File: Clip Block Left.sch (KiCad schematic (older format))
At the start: 27 parts, among them J1 Conn_02x05_Odd_Even, SW1 B3F-5050, SW10 B3F-5050, SW11 B3F-5050, SW12 B3F-5050, SW13 B3F-5050, SW14 B3F-5050, SW15 B3F-5050, SW16 B3F-5050, SW2 B3F-5050, SW3 B3F-5050, SW4 B3F-5050, SW5 B3F-5050, SW6 B3F-5050, SW7 B3F-5050, SW8 B3F-5050, SW9 B3F-5050, U1 CD74HC4067M

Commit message: All subsidiary boards complete
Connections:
- wire segments 182 -> 183
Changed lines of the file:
@@
 	1900 2450 2200 2450
-Wire Wire Line
-	1750 2250 2200 2250
 Wire Wire Line
 	2000 1150 2700 1150
@@
 	1    0    0    -1
 $EndComp
-Wire Wire Line
-	1600 2150 2200 2150
-Wire Wire Line
-	1750 2250 1750 1750
-Wire Wire Line
-	1750 1750 900  1750
-Wire Wire Line
-	900  1750 900  2150
-Wire Wire Line
-	900  2150 1100 2150
 Wire Wire Line
 	1700 2350 1700 2250
@@
 NoConn ~ 1900 4300
 NoConn ~ 1900 4800
+Wire Wire Line
+	2200 2150 2200 1900
+Wire Wire Line
+	2200 1900 900  1900
+Wire Wire Line
+	900  1900 900  2150
+Wire Wire Line
+	900  2150 1100 2150
+Wire Wire Line
+	1600 2150 1850 2150
+Wire Wire Line
+	1850 2150 1850 2250
+Wire Wire Line
+	1850 2250 2200 2250
 $EndSCHEMATC

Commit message: Housekeeping
Cleaned up the schematic for the subsidiary boards

Switched 5v and Com connections to make routing easier.
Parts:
- J1: symbol Connector_Generic:Conn_02x05_Odd_Even -> Connector:Conn_01x10_Male
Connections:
- wire segments 183 -> 172
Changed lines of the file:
@@
 	1    0    0    -1
 $EndComp
-Wire Wire Line
-	2100 2550 2100 1750
-Wire Wire Line
-	2100 1750 2200 1750
 Connection ~ 2700 1150
 NoConn ~ 4900 2450
@@
 	2200 3450 2700 3450
 Wire Wire Line
-	1750 2550 2100 2550
-Wire Wire Line
-	1900 2450 2200 2450
-Wire Wire Line
-	2000 1150 2700 1150
-Wire Wire Line
-	2000 1150 2000 2650
-Wire Wire Line
 	2700 1150 2700 1250
 Wire Wire Line
@@
 	2450 5300 2450 6100
 $Comp
-L Connector_Generic:Conn_02x05_Odd_Even J1
+L Connector:Conn_01x10_Male J1
 U 1 1 5D5B6BD9
-P 1300 2350
-F 0 "J1" H 1350 2767 50  0000 C CNN
-F 1 "Conn_02x05_Odd_Even" H 1350 2676 50  0000 C CNN
-F 2 "Connector_PinHeader_2.54mm:PinHeader_2x05_P2.54mm_Vertical" H 1300 2350 50  0001 C CNN
-F 3 "~" H 1300 2350 50  0001 C CNN
-	1    1300 2350
-	1    0    0    -1
-$EndComp
-Wire Wire Line
-	1700 2350 1700 2250
-Wire Wire Line
-	1700 2250 1600 2250
-Wire Wire Line
-	1700 2350 2200 2350
-Wire Wire Line
-	1900 2450 1900 1600
-Wire Wire Line
-	1900 1600 650  1600
-Wire Wire Line
-	650  1600 650  2250
-Wire Wire Line
-	650  2250 1100 2250
-Wire Wire Line
-	1750 2550 1750 2400
-Wire Wire Line
-	1750 2400 1650 2400
-Wire Wire Line
-	1650 2400 1650 2350
-Wire Wire Line
-	1650 2350 1600 2350
-Wire Wire Line
-	950  2650 950  2350
-Wire Wire Line
-	950  2350 1100 2350
-Wire Wire Line
-	950  2650 2000 2650
+P 750 2550
+F 0 "J1" H 750 3100 50  0000 C CNN
+F 1 "Conn_02x05_Odd_Even" H 800 2876 50  0001 C CNN
+F 2 "Connector_PinHeader_2.54mm:PinHeader_2x05_P2.54mm_Vertical" H 750 2550 50  0001 C CNN
+F 3 "~" H 750 2550 50  0001 C CNN
+	1    750  2550
+	1    0    0    -1
+$EndComp
 $Comp
 L Connector_Generic:Conn_02x03_Odd_Even JX01
@@
 NoConn ~ 750  7050
 Wire Wire Line
-	1900 3900 1700 3900
-Wire Wire Line
-	1700 3900 1700 2450
-Wire Wire Line
-	1600 2450 1700 2450
-Wire Wire Line
-	1900 4400 1600 4400
-Wire Wire Line
-	1600 4400 1600 2550
-Wire Wire Line
-	1900 4900 1100 4900
-Wire Wire Line
-	1100 4900 1100 2550
-Wire Wire Line
-	1900 5300 850  5300
-Wire Wire Line
-	850  5300 850  2450
-Wire Wire Line
-	850  2450 1100 2450
+	1900 4400 1800 4400
+Wire Wire Line
+	1900 4900 1700 4900
+Wire Wire Line
+	1900 5300 1500 5300
 NoConn ~ 1900 3800
 NoConn ~ 1900 4300
 NoConn ~ 1900 4800
 Wire Wire Line
-	2200 2150 2200 1900
-Wire Wire Line
-	2200 1900 900  1900
-Wire Wire Line
-	900  1900 900  2150
-Wire Wire Line
-	900  2150 1100 2150
-Wire Wire Line
-	1600 2150 1850 2150
-Wire Wire Line
-	1850 2150 1850 2250
-Wire Wire Line
-	1850 2250 2200 2250
+	2200 2150 950  2150
+Wire Wire Line
+	950  2250 2200 2250
+Wire Wire Line
+	950  2550 1700 2550
+Wire Wire Line
+	1700 2550 1700 1750
+Wire Wire Line
+	1700 1750 2200 1750
+Wire Wire Line
+	950  2650 1500 2650
+Wire Wire Line
+	1500 2650 1500 1150
+Wire Wire Line
+	1500 1150 2700 1150
+Wire Wire Line
+	1900 2450 950  2450
+Wire Wire Line
+	2200 2350 2100 2350
+Wire Wire Line
+	2200 2450 2100 2450
+Wire Wire Line
+	1900 2350 2100 2450
+Wire Wire Line
+	1900 2450 2100 2350
+Wire Wire Line
+	950  2350 1900 2350
+Wire Wire Line
+	950  2750 1500 2750
+Wire Wire Line
+	1500 2750 1500 5300
+Wire Wire Line
+	950  2850 1600 2850
+Wire Wire Line
+	1600 2850 1600 3900
+Wire Wire Line
+	1600 3900 1900 3900
+Wire Wire Line
+	950  2950 1700 2950
+Wire Wire Line
+	1700 2950 1700 4900
+Wire Wire Line
+	950  3050 1800 3050
+Wire Wire Line
+	1800 3050 1800 4400
 $EndSCHEMATC

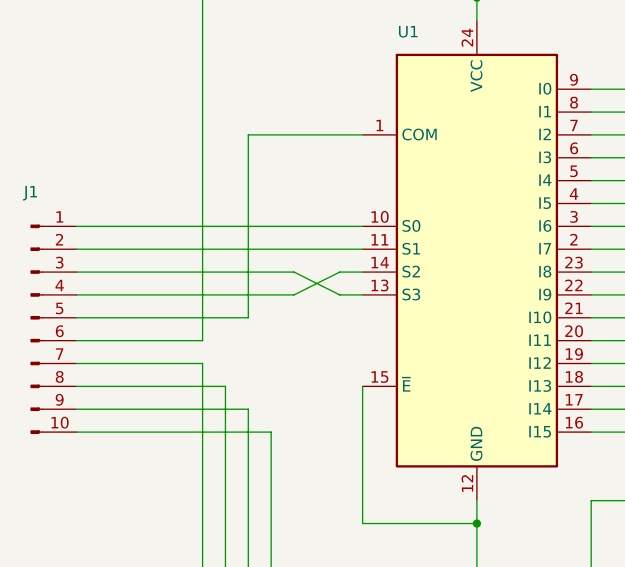
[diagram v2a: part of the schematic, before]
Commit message: Fixed S0-S3 Rail, added LEDS
Was an error on the schematic, easily fixed without changing the traces, glad I left it before deleting them all.

LEDs and relate resistors are in.
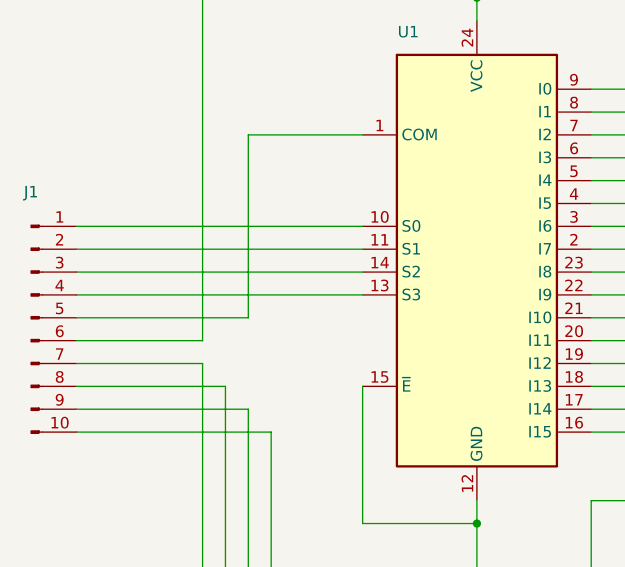
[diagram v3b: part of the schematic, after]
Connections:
- net at U1.13 (S3): now also J1.4 (Pin_4); no longer J1.3 (Pin_3)
- net at U1.14 (S2): now also J1.3 (Pin_3); no longer J1.4 (Pin_4)
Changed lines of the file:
@@
 	1500 1150 2700 1150
-Wire Wire Line
-	1900 2450 950  2450
-Wire Wire Line
-	2200 2350 2100 2350
-Wire Wire Line
-	2200 2450 2100 2450
-Wire Wire Line
-	1900 2350 2100 2450
-Wire Wire Line
-	1900 2450 2100 2350
-Wire Wire Line
-	950  2350 1900 2350
 Wire Wire Line
 	950  2750 1500 2750
@@
 Wire Wire Line
 	1800 3050 1800 4400
+Wire Wire Line
+	950  2350 2200 2350
+Wire Wire Line
+	950  2450 2200 2450
 $EndSCHEMATC

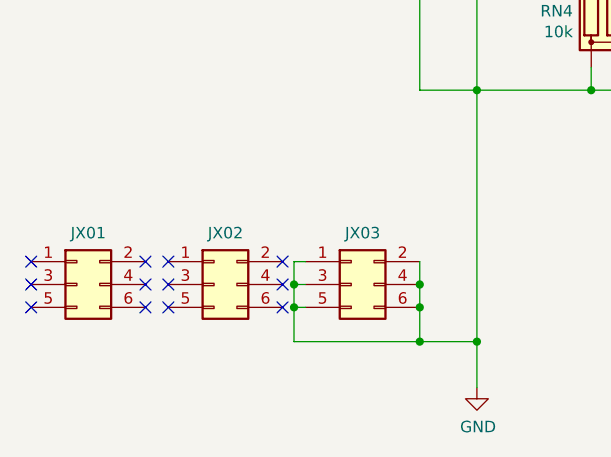
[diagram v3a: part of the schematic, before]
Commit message: Rails done, GND corrected.
Now for checking and decals
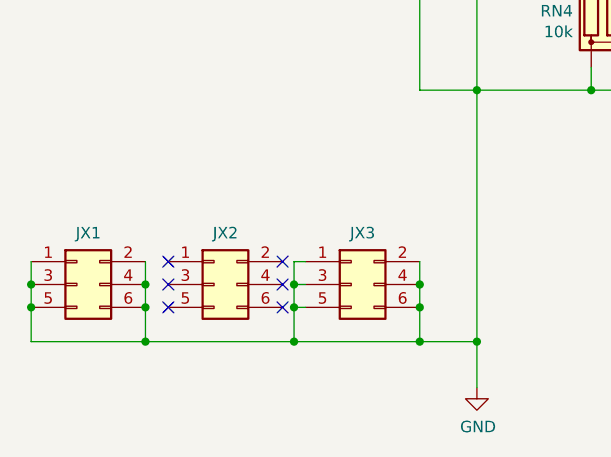
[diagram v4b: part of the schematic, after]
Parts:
- renumbered JX01 to JX1, JX02 to JX2, JX03 to JX3
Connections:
- net GND: now also JX1.1 (Pin_1), JX1.2 (Pin_2), JX1.3 (Pin_3), JX1.4 (Pin_4), JX1.5 (Pin_5), JX1.6 (Pin_6)
- no-connect marks 52 -> 46
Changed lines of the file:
@@
 $Descr A4 11693 8268
 encoding utf-8
-Sheet 6 8
+Sheet 6 9
 Title ""
 Date ""
@@
 $EndComp
 $Comp
-L Connector_Generic:Conn_02x03_Odd_Even JX01
+L Connector_Generic:Conn_02x03_Odd_Even JX1
 U 1 1 5D73B5EC
 P 950 6950
-F 0 "JX01" H 1000 7175 50  0000 C CNN
+F 0 "JX1" H 1000 7175 50  0000 C CNN
 F 1 "Conn_02x03_Odd_Even" H 1000 7176 50  0001 C CNN
 F 2 "Connector_PinHeader_2.54mm:PinHeader_2x03_P2.54mm_Vertical" H 950 6950 50  0001 C CNN
@@
 $EndComp
 $Comp
-L Connector_Generic:Conn_02x03_Odd_Even JX03
+L Connector_Generic:Conn_02x03_Odd_Even JX3
 U 1 1 5D745204
 P 2150 6950
-F 0 "JX03" H 2200 7175 50  0000 C CNN
+F 0 "JX3" H 2200 7175 50  0000 C CNN
 F 1 "Conn_02x03_Odd_Even" H 2200 7176 50  0001 C CNN
 F 2 "Connector_PinHeader_2.54mm:PinHeader_2x03_P2.54mm_Vertical" H 2150 6950 50  0001 C CNN
@@
 	2450 7050 2450 7200
 $Comp
-L Connector_Generic:Conn_02x03_Odd_Even JX02
+L Connector_Generic:Conn_02x03_Odd_Even JX2
 U 1 1 5D73B760
 P 1550 6950
-F 0 "JX02" H 1600 7175 50  0000 C CNN
+F 0 "JX2" H 1600 7175 50  0000 C CNN
 F 1 "Conn_02x03_Odd_Even" H 1600 7176 50  0001 C CNN
 F 2 "Connector_PinHeader_2.54mm:PinHeader_2x03_P2.54mm_Vertical" H 1550 6950 50  0001 C CNN
@@
 NoConn ~ 1350 6950
 NoConn ~ 1350 6850
-NoConn ~ 1250 6850
-NoConn ~ 1250 6950
-NoConn ~ 1250 7050
-NoConn ~ 750  6850
-NoConn ~ 750  6950
-NoConn ~ 750  7050
 Wire Wire Line
 	1900 4400 1800 4400
@@
 Wire Wire Line
 	950  2450 2200 2450
+Wire Wire Line
+	1250 6850 1250 6950
+Wire Wire Line
+	1250 7200 1900 7200
+Connection ~ 1250 6950
+Wire Wire Line
+	1250 6950 1250 7050
+Connection ~ 1250 7050
+Wire Wire Line
+	1250 7050 1250 7200
+Connection ~ 1900 7200
+Wire Wire Line
+	750  6850 750  6950
+Wire Wire Line
+	750  7200 1250 7200
+Connection ~ 750  6950
+Wire Wire Line
+	750  6950 750  7050
+Connection ~ 750  7050
+Wire Wire Line
+	750  7050 750  7200
+Connection ~ 1250 7200
 $EndSCHEMATC
